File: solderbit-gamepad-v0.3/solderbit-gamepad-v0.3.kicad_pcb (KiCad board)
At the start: 2 copper layers, 97.8 x 35 mm, 28 parts, among them U1 74HC165D_653

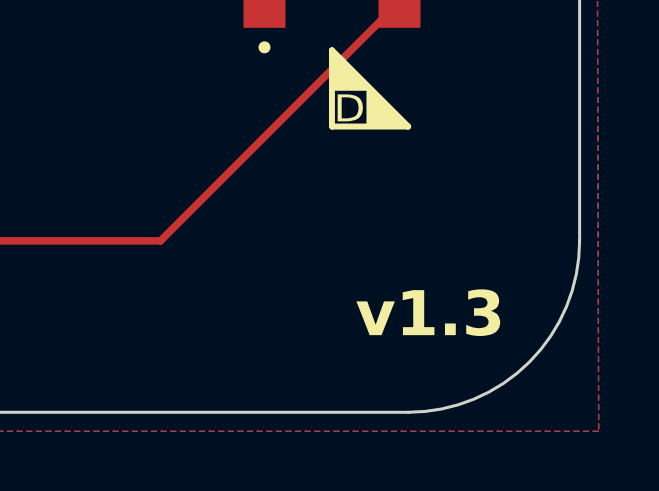
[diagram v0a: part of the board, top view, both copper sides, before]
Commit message: Begin version 0.7, and new spreadsheet
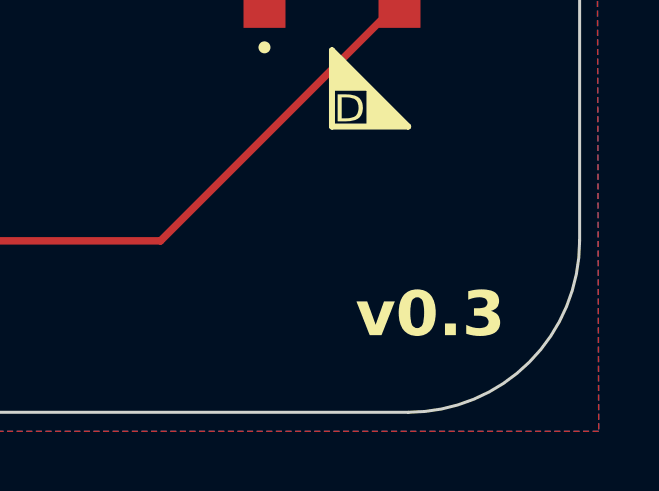
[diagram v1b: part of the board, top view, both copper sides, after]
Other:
- board text added: "v0.3"
- board text removed: "v1.3"
